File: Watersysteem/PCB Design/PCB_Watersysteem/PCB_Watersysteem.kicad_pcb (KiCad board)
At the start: 2 copper layers, 73 x 124 mm, 99 parts, among them J1 12V ingang, J10 LED Water Level, J11 LED Nutrient Level, J12 Height Nutrients, J13 Height Mixer, J14 Pomp1, J15 Pomp2, J16 Pomp3, J17 Pomp4, J18 Luchtpomp, J19 Mixer, J2 TTL Connector, J20 UV, J22 230V, J23 ReferentieProbe, J24 Voedingsstoffen 1, J25 Voedingsstoffen 2, J26 Voedingsstoffen 3, J3 Backup GPIO, J4 TestPins, J6 Height Water, J7 Endstop Lade0, J8 Endstop Lade1, J9 Endstop UV, K1 AHQSS105DM2FA0G, K2 AHQSS105DM2FA0G, K3 AHQSS105DM2FA0G, K6 AHQSS105DM2FA0G, K7 AHQSS105DM2FA0G, K8 AHQSS105DM2FA0G, K9 AHQSS105DM2FA0G, Q1 BSS138, Q2 BSS138, Q3 BSS138, Q4 BSS138, Q5 BSS138, Q6 BSS138, Q7 BSS138, SW1 EN, SW2 BOOT, U1 ESP32-WROOM-32D, U2 MP1584_Module, U3 AMS1117-3.3, U4 ADS1115IDGS, U5 MCP23017_SO

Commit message: PCB Update
samenbrengen designs, polarisaties plaatsen
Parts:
- H2: value MountingHole_Pad -> MountingHole; footprint MountingHole:MountingHole_3.2mm_M3_Pad_TopBottom -> MountingHole:MountingHole_3.2mm_M3
- moved TP1 14.0 mm to (94.1, 126.0)
- moved TP3 2.01 mm to (95.3, 140.3)
- moved TP2 1.49 mm to (95.8, 130.5)
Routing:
- net 3V3: track 170.9 -> 174.4 mm
- net RefProbe: track 41.4 -> 38.5 mm
- net Nutr2: track 9.15 -> 7.42 mm
- net Nutr1: track 22.9 -> 24.4 mm
- net GND: vias 48 -> 52
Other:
- board text added: "- +"
- board text added: "Ref"
- board text added: "Rev1"
- board text added: "WayWayWay"

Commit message: Update PCB
Logotje toegevoegd
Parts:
- added G***: LOGO, LOGO, F.Cu at (85.2, 150.4)

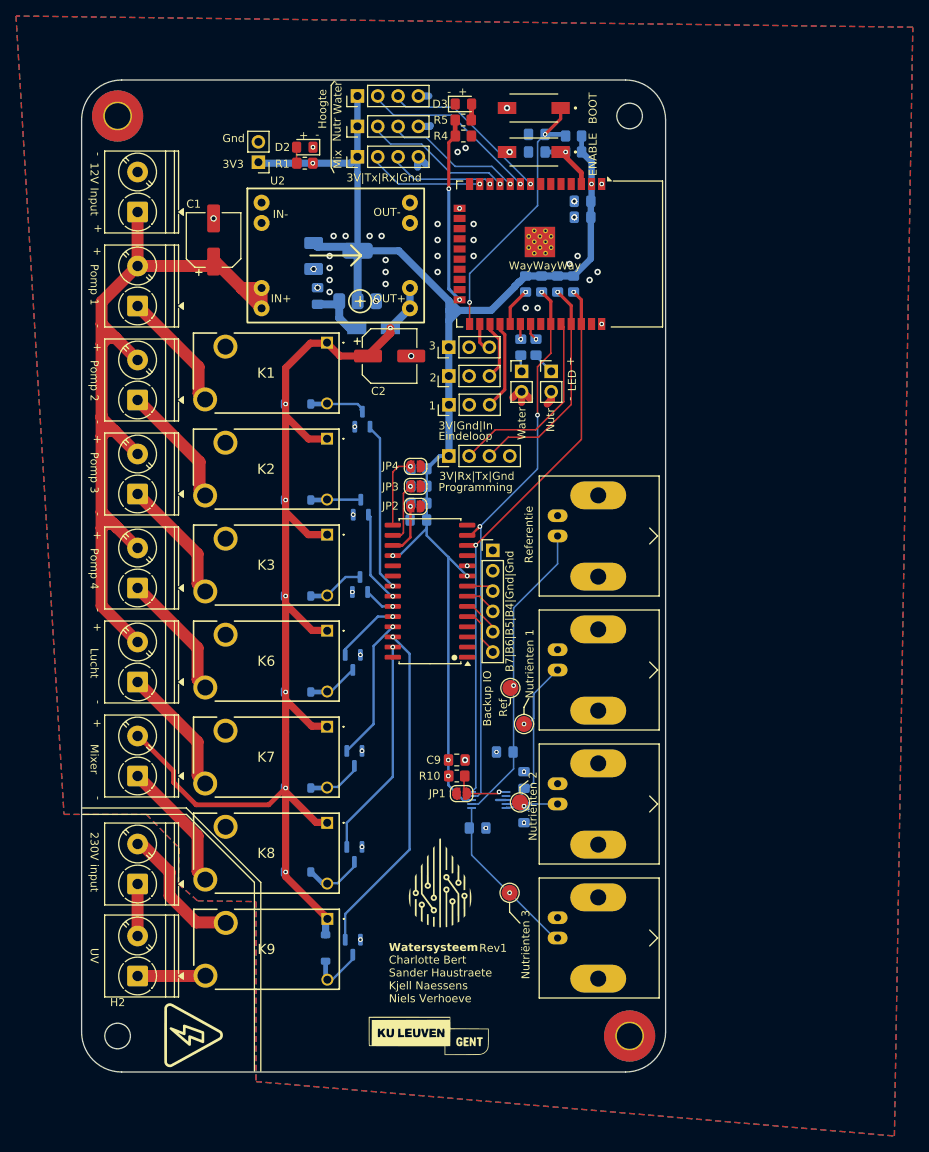
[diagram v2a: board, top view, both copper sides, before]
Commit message: Update PCB
Afmetingen verkleind (100x100), rerouting, clean-up
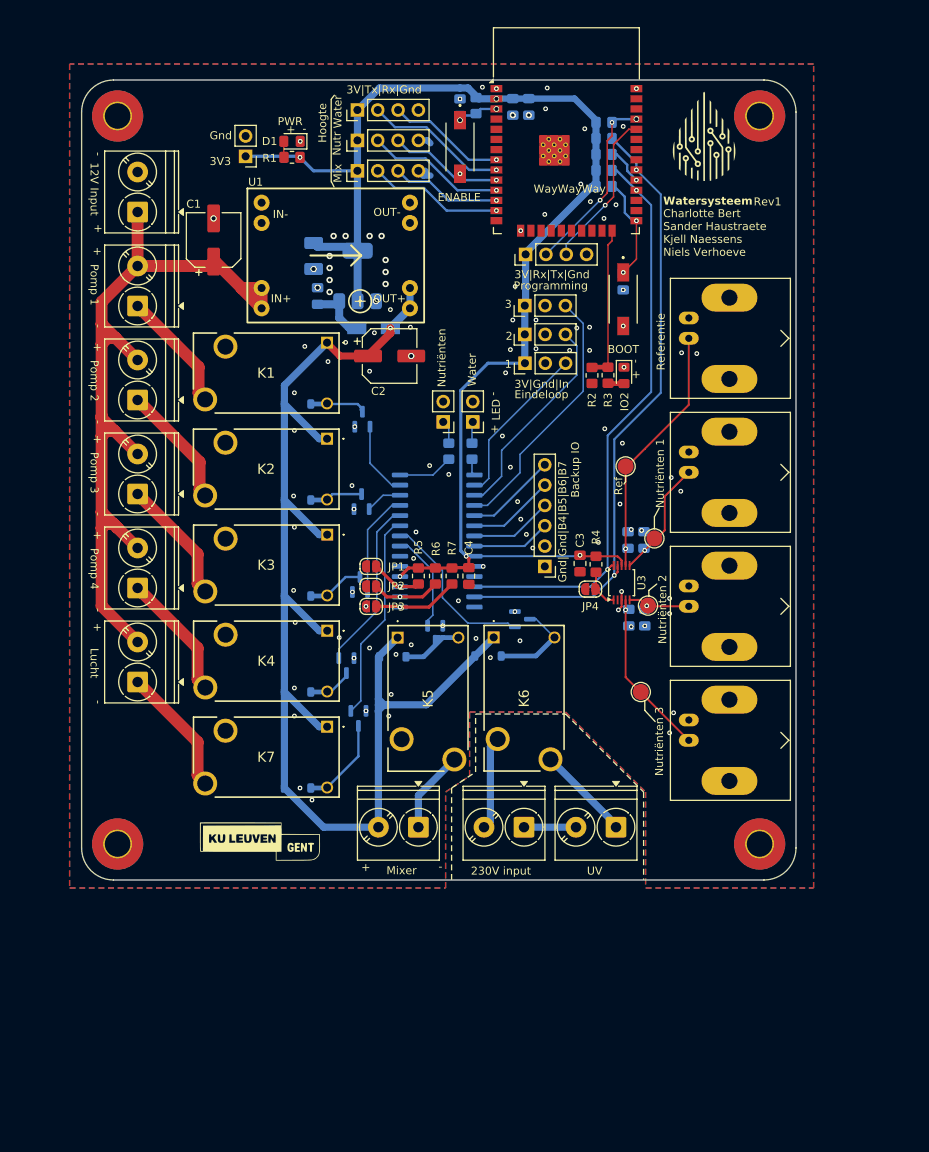
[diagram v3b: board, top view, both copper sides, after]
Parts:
- C4: renamed from C14; moved to F.Cu
- G***, U5: moved to B.Cu
- H2, H3: value MountingHole -> MountingHole_Pad; footprint MountingHole:MountingHole_3.2mm_M3 -> MountingHole:MountingHole_3.2mm_M3_Pad_TopBottom
- R5: renamed from R13; moved to F.Cu
- R6: renamed from R12; moved to F.Cu
- R7: renamed from R11; moved to F.Cu
- U3: renamed from U4; moved to F.Cu
- moved H2 140.2 mm to (125.2, 54.5)
- moved G*** 127.9 mm to (118.1, 58.4), turned to 180 degrees
- moved H3 111.3 mm to (45.0, 145.5)
- moved G*** 99.0 mm to (118.2, 57.1)
- moved G*** 63.7 mm to (106.4, 132.6), turned to 180 degrees
- moved J24 62.6 mm to (107.3, 143.4), turned to 180 degrees
- moved J23 48.8 mm to (95.8, 143.4), turned to 180 degrees
- moved Q4 46.2 mm to (95.6, 117.4), turned to 0 degrees
- moved D7 41.8 mm to (91.3, 122.0), turned to 0 degrees
- moved K6 40.9 mm to (92.0, 119.7), turned to -90 degrees
- moved D2 39.4 mm to (108.3, 86.9), turned to -90 degrees
- moved R3 36.7 mm to (106.3, 86.9), turned to -90 degrees
- moved J22 35.7 mm to (82.6, 143.4), turned to 180 degrees
- moved R2 34.0 mm to (104.3, 86.9), turned to -90 degrees
- moved C11 33.5 mm to (110.8, 107.5)
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- renumbered C8 to C10, C13 to C11, C10 to C12, C11 to C13, C12 to C14, C9 to C3, C4 to C8, C3 to C9, D2 to D1, D13 to D10, D3 to D2, D1 to D3, D7 to D4, D8 to D5, D9 to D6, D12 to D7, D11 to D8, D10 to D9, J6 to J1, J23 to J10, J7 to J11, J15 to J12, J10 to J13, J11 to J14, J24 to J15, J3 to J18, J25 to J19, J12 to J2, J18 to J20, J26 to J21, J19 to J22, J22 to J23, J20 to J24, J13 to J3, J1 to J5, J14 to J6, J2 to J7, J9 to J8, J8 to J9, JP2 to JP1, JP3 to JP2, JP4 to JP3, JP1 to JP4, K6 to K4, K8 to K5, K9 to K6, Q6 to Q4, Q7 to Q5, Q4 to Q6, Q5 to Q7, R8 to R10, R7 to R11, R9 to R12, R3 to R13, R15 to R14, R14 to R15, R4 to R2, R5 to R3, R10 to R4, R6 to R8, R2 to R9, U2 to U1, U1 to U2, U3 to U4
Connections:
- J7 pad 2: RX0 -> TX0
- J7 pad 3: TX0 -> RX0
- U2 pad 26: ENDSTOP3 -> unconnected-(U2-IO4-Pad26)
- U2 pad 27: ENDSTOP2 -> unconnected-(U2-IO16-Pad27)
- U2 pad 28: ENDSTOP1 -> SCL0
- U2 pad 30: LED WATER -> SDA0
- U2 pad 31: LED NUTR -> unconnected-(U2-IO19-Pad31)
- U2 pad 33: SDA0 -> unconnected-(U2-IO21-Pad33)
- U2 pad 36: SCL0 -> unconnected-(U2-IO22-Pad36)
- U3 pad 4: Nutr1 -> Nutr3
- U3 pad 6: Nutr3 -> Nutr1
- U5 pad 1: unconnected-(U5-GPB0-Pad1) -> LED NUTR
- U5 pad 2: unconnected-(U5-GPB1-Pad2) -> ENDSTOP1
- U5 pad 21: RELAY_PUMP1 -> RELAY_MIXER
- U5 pad 22: RELAY_PUMP2 -> RELAY_UV
- U5 pad 23: RELAY_PUMP3 -> RELAY_AIR
- U5 pad 25: RELAY_AIR -> RELAY_PUMP3
- U5 pad 26: RELAY_UV -> RELAY_PUMP2
- U5 pad 27: RELAY_MIXER -> RELAY_PUMP1
- U5 pad 28: unconnected-(U5-GPA7-Pad28) -> LED WATER
- U5 pad 3: unconnected-(U5-GPB2-Pad3) -> ENDSTOP2
- U5 pad 4: unconnected-(U5-GPB3-Pad4) -> ENDSTOP3
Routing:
- net ENDSTOP3: track 4.08 -> 32.5 mm
- net GPIO0: track 34.4 -> 13.1 mm
- net RELAY_UV: track 42.1 -> 21.1 mm, vias 1 -> 0
- net ENDSTOP2: track 7.52 -> 26.6 mm
- net RELAY_MIXER: track 27.4 -> 12.5 mm, vias 1 -> 0
- net RELAY_PUMP4: track 8.35 -> 21.5 mm, vias 1 -> 0
- net RELAY_PUMP1: track 21.1 -> 9.46 mm, vias 1 -> 0
- net Nutr1: track 24.4 -> 14.7 mm
- net 5V: track 152.6 -> 162.0 mm, vias 7 -> 1
- net ENDSTOP1: track 11.1 -> 20.5 mm
- net SDA0: track 70.2 -> 79.6 mm, vias 3 -> 2
- net RELAY_PUMP3: track 3.90 -> 13.1 mm, vias 1 -> 0
- net RELAY_AIR: track 17.9 -> 26.1 mm, vias 1 -> 0
- net RELAY_PUMP2: track 11.6 -> 4.57 mm, vias 1 -> 0
- net RefProbe: track 38.5 -> 31.7 mm
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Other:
- board size 73 x 124 mm -> 89.3 x 100 mm
- board text added: "DO NOT EAT!"
- board text added: "Gnd|Gnd|B4|B5|B6|B7"
- board text added: "IO2"
- board text added: "Nutriënten"
- board text added: "PWR"
- board text removed: "B7|B6|B5|B4|Gnd|Gnd"

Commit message: Update PCB
Extra eindwerk rond vias en silkscreen
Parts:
- added G***: LOGO, LOGO, F.Cu at (115.2, 144.6)
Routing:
- net GND: vias 112 -> 113
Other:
- board text added: "What are you looking for?"

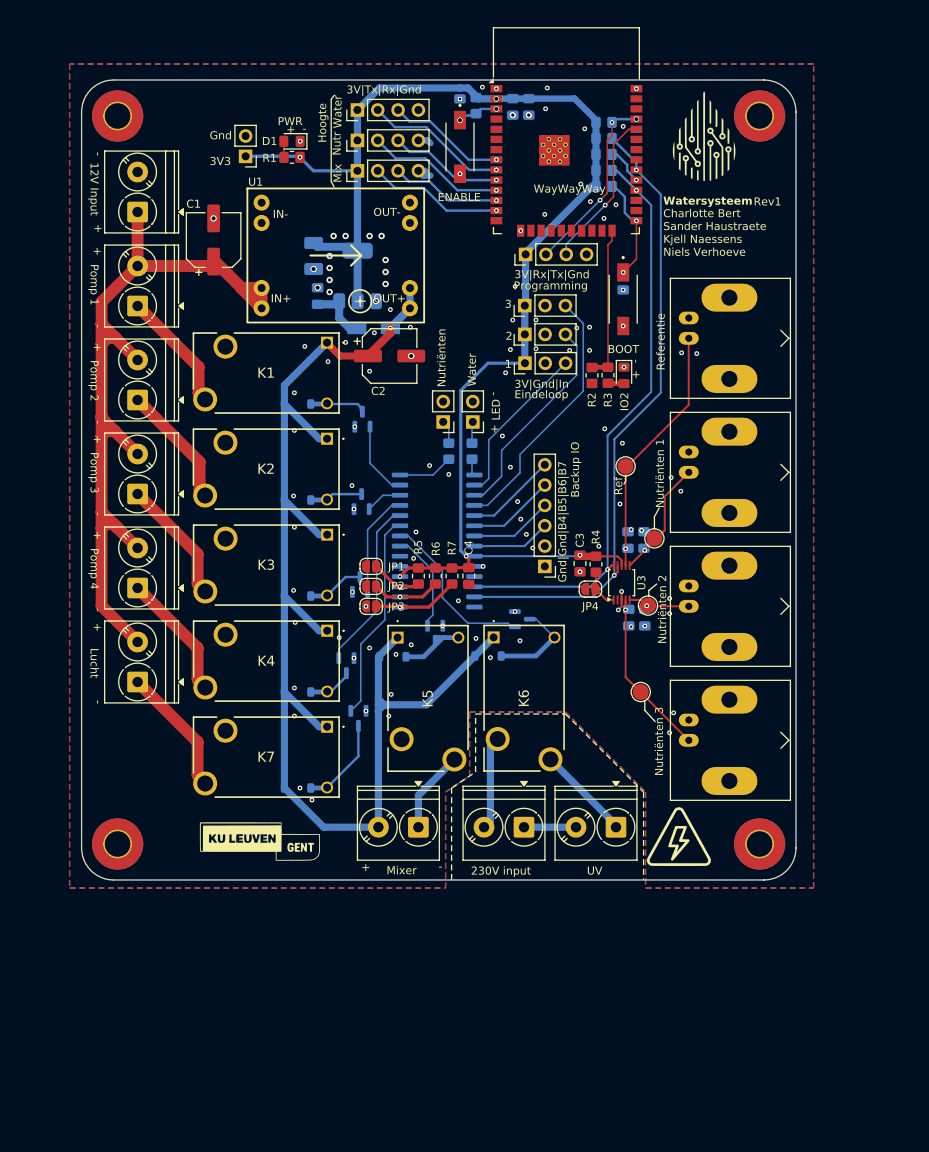
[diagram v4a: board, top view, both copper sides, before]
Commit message: Update PCB
Eindwerk aan PCB (extra vias, meer silkscreen, lichte aanpassing floorplanning,...)
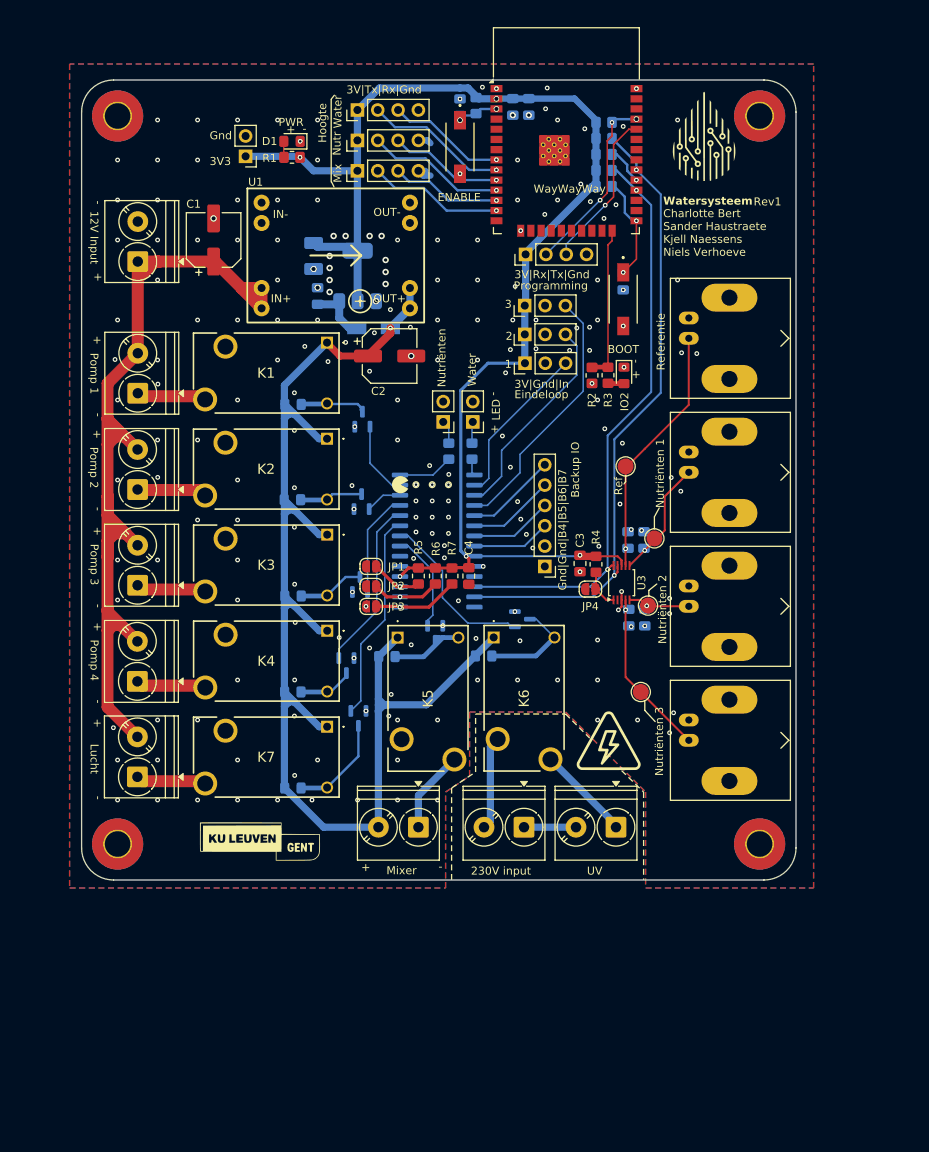
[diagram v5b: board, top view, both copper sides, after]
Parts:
- added G***: LOGO, LOGO, F.Cu at (80.3, 100.6)
- added G***: LOGO, LOGO, B.Cu at (118.0, 67.1)
- D10, D4, D5, D6, D7, D8, D9: value 1N4148W -> 1N4148; footprint Diode_SMD:D_SOD-123 -> Diode_SMD:D_0805_2012Metric_Pad1.15x1.40mm_HandSolder
- moved G*** 14.9 mm to (106.4, 132.6)
- moved J20 11.9 mm to (47.5, 137.1)
- moved J17 11.7 mm to (47.5, 125.2)
- moved J16 11.4 mm to (47.5, 113.2)
- moved J12 11.2 mm to (47.5, 101.2)
- moved J6 10.9 mm to (47.5, 89.2)
- moved J5 6.19 mm to (47.5, 72.7)
- moved D8 0.74 mm to (78.7, 122.1)
- moved D5 0.65 mm to (66.9, 102.5)
- moved D9 0.60 mm to (66.9, 126.5)
- moved D10 0.59 mm to (66.9, 138.5)
- moved D4 0.57 mm to (66.9, 90.6)
- moved D6 0.57 mm to (66.9, 114.5)
- moved D7 0.55 mm to (90.8, 122.0)
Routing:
- net 12V: track 106.4 -> 117.7 mm
- net AIR: track 16.2 -> 8.87 mm
- net PUMP4: track 15.9 -> 8.83 mm
- net PUMP3: track 15.7 -> 8.78 mm
- net PUMP2: track 15.4 -> 8.79 mm
- net PUMP1: track 15.2 -> 8.74 mm
- net 5V: track 162.0 -> 168.2 mm
- net Net-(D8-A): track 8.66 -> 10.0 mm
- net Net-(D5-A): track 6.74 -> 8.02 mm
- net Net-(D4-A): track 7.12 -> 8.36 mm
- net Net-(D9-A): track 5.66 -> 6.89 mm
- net Net-(D10-A): track 11.4 -> 12.6 mm
- net Net-(D6-A): track 7.13 -> 8.33 mm
- net Net-(D7-A): track 11.6 -> 12.8 mm
- net GND: vias 113 -> 215
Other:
- board text added: "DO NOT WATER!"
- board text added: "UNSAFE BUT FUN"
